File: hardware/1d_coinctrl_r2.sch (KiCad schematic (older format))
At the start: 14 parts, among them J1 +12V INPUT, J2 CO LINE, J3 V_RLY_SEL, J4 TEL LINE, J5 COIN LINE, J7 Conn_01x02

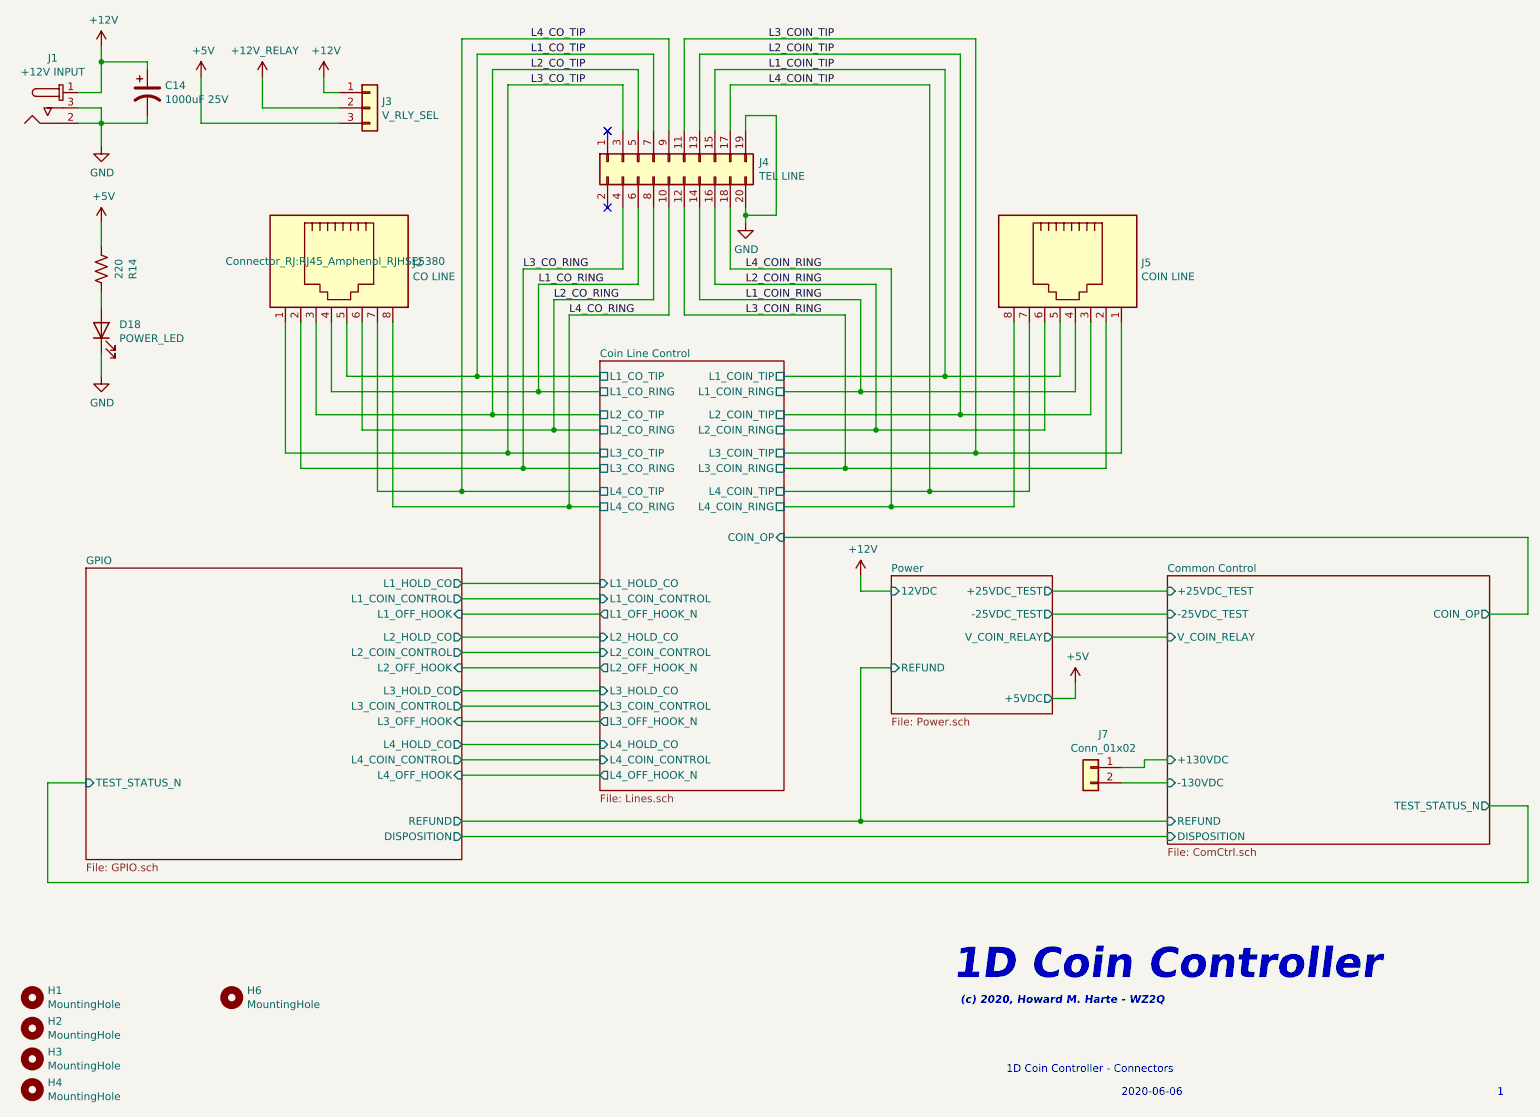
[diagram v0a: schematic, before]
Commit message: Issue 2 schmatic and Layout
Added polarity reversal detection to monitor answer supervision.
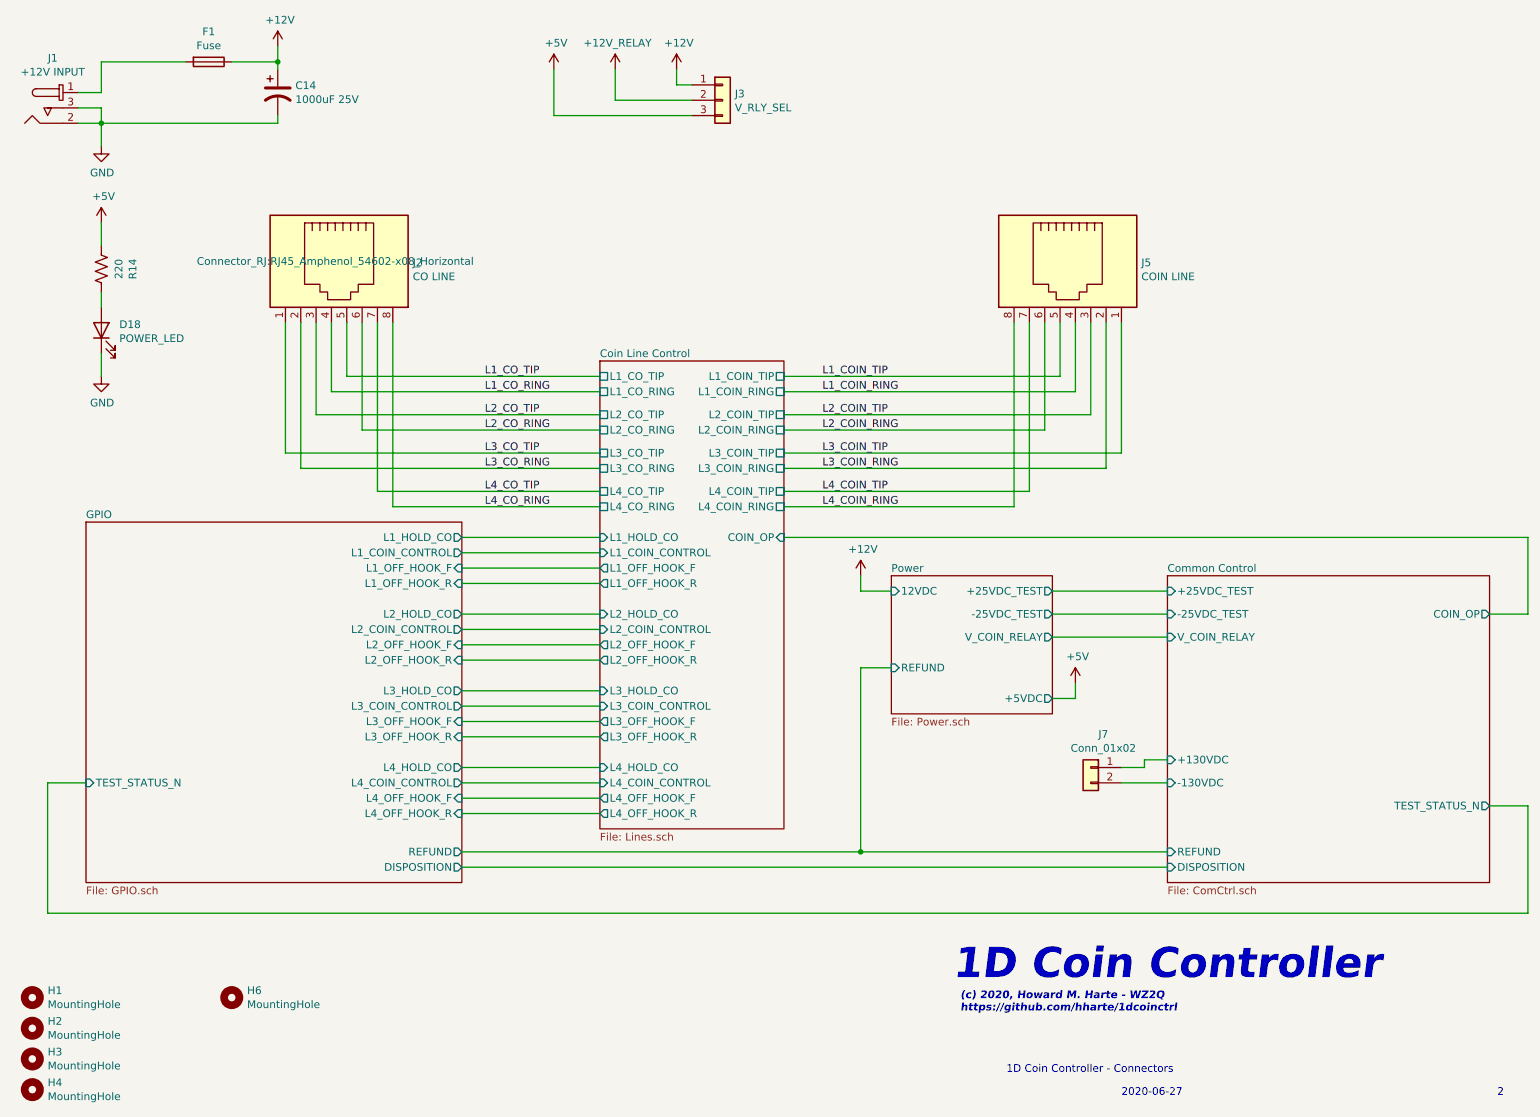
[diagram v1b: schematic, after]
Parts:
- removed J4: TEL LINE, Connector_PinHeader_2.54mm:PinHeader_2x10_P2.54mm_Vertical, symbol Connector_Generic:Conn_02x10_Odd_Even
- added F1: Fuse, Resistor_THT:R_Axial_DIN0207_L6.3mm_D2.5mm_P10.16mm_Horizontal, symbol Device:Fuse
- J2, J5: footprint Connector_RJ:RJ45_Amphenol_RJHSE5380 -> Connector_RJ:RJ45_Amphenol_54602-x08_Horizontal
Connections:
- net +12V: now also F1.1; no longer J1.1
- new net: F1.2, J1.1
- no-connect marks 2 -> 0
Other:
- note added: "(c) 2020, Howard M. Harte - WZ2Q\nhttps://github.com/hharte/1dcoinctrl"
- note added: "2"
- note added: "2020-06-27"
- note removed: "(c) 2020, Howard M. Harte - WZ2Q"
- note removed: "1"
- note removed: "2020-06-06"
- moved on the sheet: C14, J3
